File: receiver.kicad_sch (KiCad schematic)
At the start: 146 parts, among them U1 AD8334ACPZ, U4 AD8334ACPZ, U8 TLV9354IDR, U9 TLV9354IDR

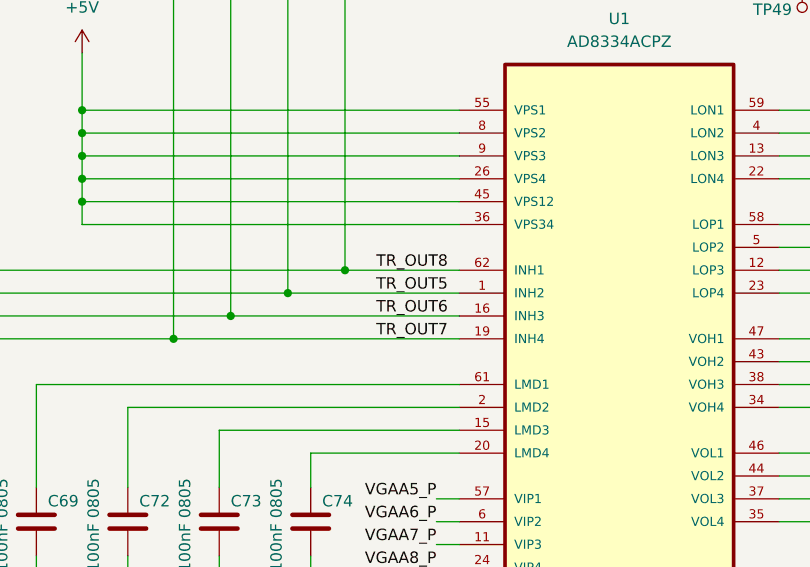
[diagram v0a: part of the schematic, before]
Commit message: 1/4 AFE edits left to go, check if MCU ADC channels could be swapped (use oth ADCs), add voltage monitoring & power planes
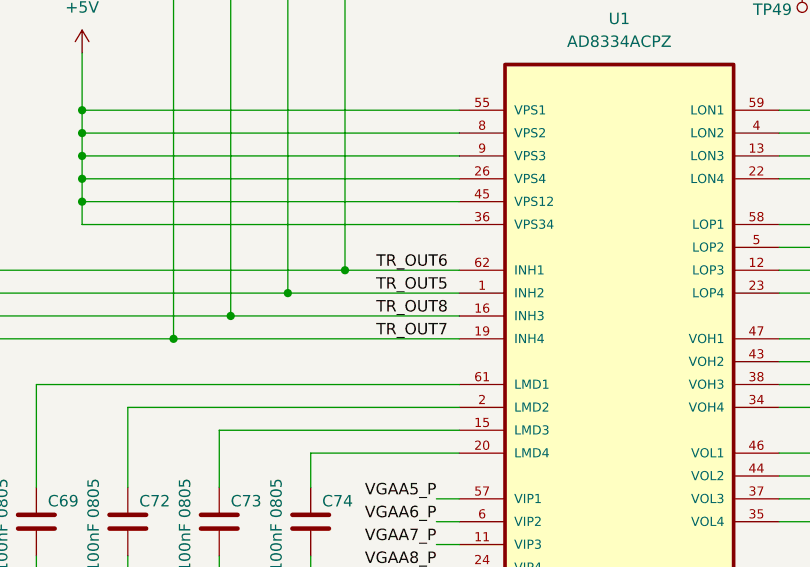
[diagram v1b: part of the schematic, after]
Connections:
- net TR_OUT6: no longer C63.1, R45.1, U1.16 (INH3)
- new net TR_OUT8: C63.1, R45.1, U1.16 (INH3)
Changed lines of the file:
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@@
 	)
 	(label "TR_OUT6"
-		(at 306.07 72.39 180)
+		(at 306.07 67.31 180)
 		(effects
 			(font
@@
 	)
 	(label "TR_OUT8"
-		(at 306.07 67.31 180)
-		(effects
-			(font
+		(at 306.07 72.39 180)
+		(effects
+			(font

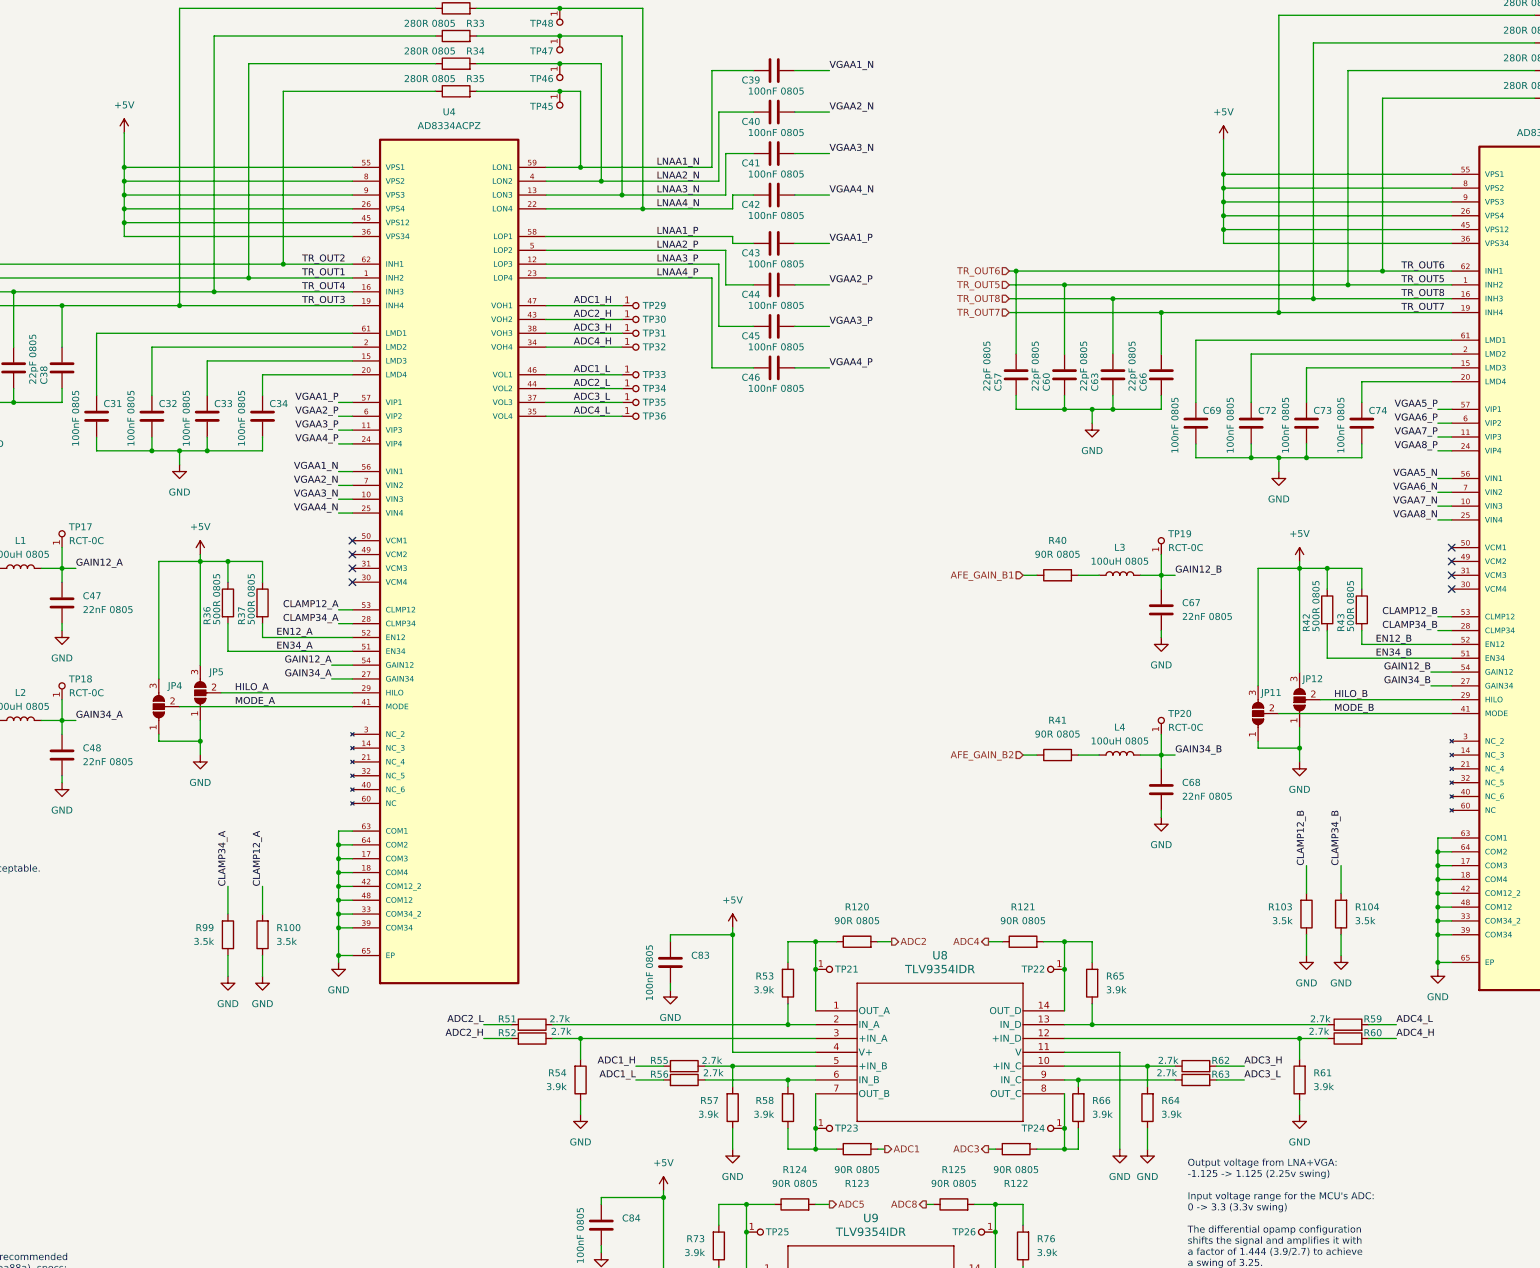
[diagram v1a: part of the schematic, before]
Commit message: 5% left, rearrange ADC channels for right AFE
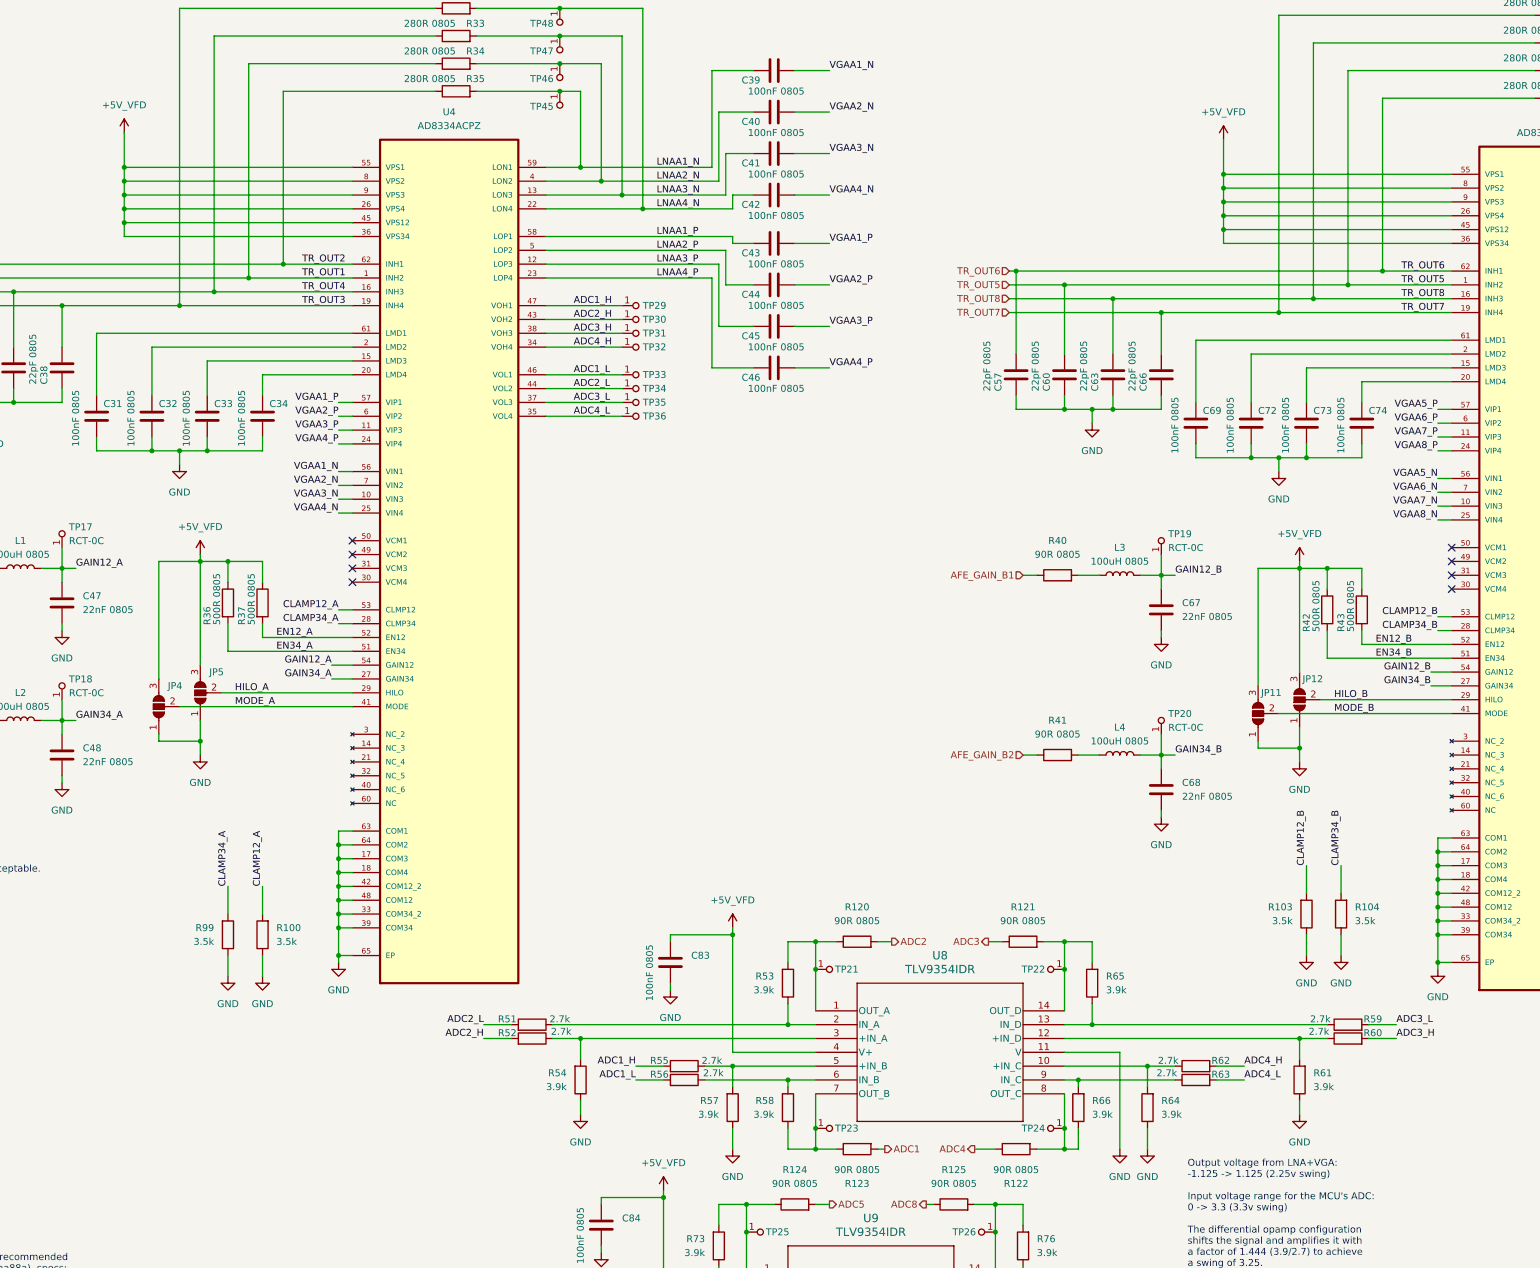
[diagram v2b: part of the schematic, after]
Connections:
- net ADC3: now also R121.1; no longer R122.1
- net ADC3_H: now also R60.2; no longer R62.2
- net ADC3_L: now also R59.2; no longer R63.2
- net ADC4: now also R122.1; no longer R121.1
- net ADC4_H: now also R62.2; no longer R60.2
- net ADC4_L: now also R63.2; no longer R59.2
- net +5V renamed +5V_VFD
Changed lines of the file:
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@@
 	(wire
 		(pts
-			(xy 222.25 228.6) (xy 223.52 228.6)
+			(xy 219.71 228.6) (xy 223.52 228.6)
 		)
 		(stroke
@@
 		)
 	)
+	(label "ADC3_H"
+		(at 297.18 208.28 0)
+		(effects
+			(font
+				(size 1.27 1.27)
+			)
+			(justify left bottom)
+		)
+	)
 	(label "VGAA1_N"
 		(at 102.87 104.14 180)
@@
 		)
 	)
-	(label "ADC3_L"
-		(at 269.24 215.9 0)
-		(effects
-			(font
-				(size 1.27 1.27)
-			)
-			(justify left bottom)
-		)
-	)
 	(label "CLAMP12_A"
 		(at 102.87 129.54 180)
@@
 		)
 	)
-	(label "LNAA3_P"
-		(at 161.29 66.04 0)
+	(label "ADC4_L"
+		(at 269.24 215.9 0)
 		(effects
 			(font
@@
 		)
 	)
-	(label "ADC7_L"
-		(at 256.54 264.16 0)
+	(label "LNAA3_P"
+		(at 161.29 66.04 0)
 		(effects
 			(font
@@
 	)
 	(label "ADC7_L"
-		(at 347.98 92.71 0)
+		(at 256.54 264.16 0)
 		(effects
 			(font
@@
 		)
 	)
-	(label "ADC3_H"
-		(at 269.24 213.36 0)
+	(label "ADC7_L"
+		(at 347.98 92.71 0)
 		(effects
 			(font
@@
 		)
 	)
-	(label "ADC4_L"
-		(at 297.18 205.74 0)
-		(effects
-			(font
-				(size 1.27 1.27)
-			)
-			(justify left bottom)
-		)
-	)
 	(label "GAIN12_B"
 		(at 303.53 140.97 180)
@@
 		)
 	)
+	(label "ADC4_H"
+		(at 269.24 213.36 0)
+		(effects
+			(font
+				(size 1.27 1.27)
+			)
+			(justify left bottom)
+		)
+	)
 	(label "CLAMP34_A"
 		(at 102.87 132.08 180)
@@
 		)
 	)
-	(label "ADC4_H"
-		(at 297.18 208.28 0)
-		(effects
-			(font
-				(size 1.27 1.27)
-			)
-			(justify left bottom)
-		)
-	)
 	(label "ADC3_H"
 		(at 146.05 78.74 0)
@@
 		)
 	)
+	(label "ADC3_L"
+		(at 297.18 205.74 0)
+		(effects
+			(font
+				(size 1.27 1.27)
+			)
+			(justify left bottom)
+		)
+	)
 	(label "ADC5_L"
 		(at 116.84 254 180)
@@
 	(hierarchical_label "ADC3"
 		(shape output)
-		(at 222.25 228.6 180)
+		(at 222.25 190.5 180)
 		(effects
 			(font
@@
 	(hierarchical_label "ADC4"
 		(shape output)
-		(at 222.25 190.5 180)
+		(at 219.71 228.6 180)
 		(effects
 			(font
@@
 			)
 		)
-		(property "Value" "+5V"
+		(property "Value" "+5V_VFD"
 			(at 279.4 115.57 0)
 			(effects
@@
 			)
 		)
-		(property "Value" "+5V"
+		(property "Value" "+5V_VFD"
 			(at 77.47 114.3 0)
 			(effects
@@
 			)
 		)
-		(property "Value" "+5V"
+		(property "Value" "+5V_VFD"
 			(at 162.56 231.14 0)
 			(effects
@@
 			)
 		)
-		(property "Value" "+5V"
+		(property "Value" "+5V_VFD"
 			(at 175.26 182.88 0)
 			(effects
@@
 			)
 		)
-		(property "Value" "+5V"
+		(property "Value" "+5V_VFD"
 			(at 63.5 36.83 0)
 			(effects
@@
 			)
 		)
-		(property "Value" "+5V"
+		(property "Value" "+5V_VFD"
 			(at 265.43 38.1 0)
 			(effects

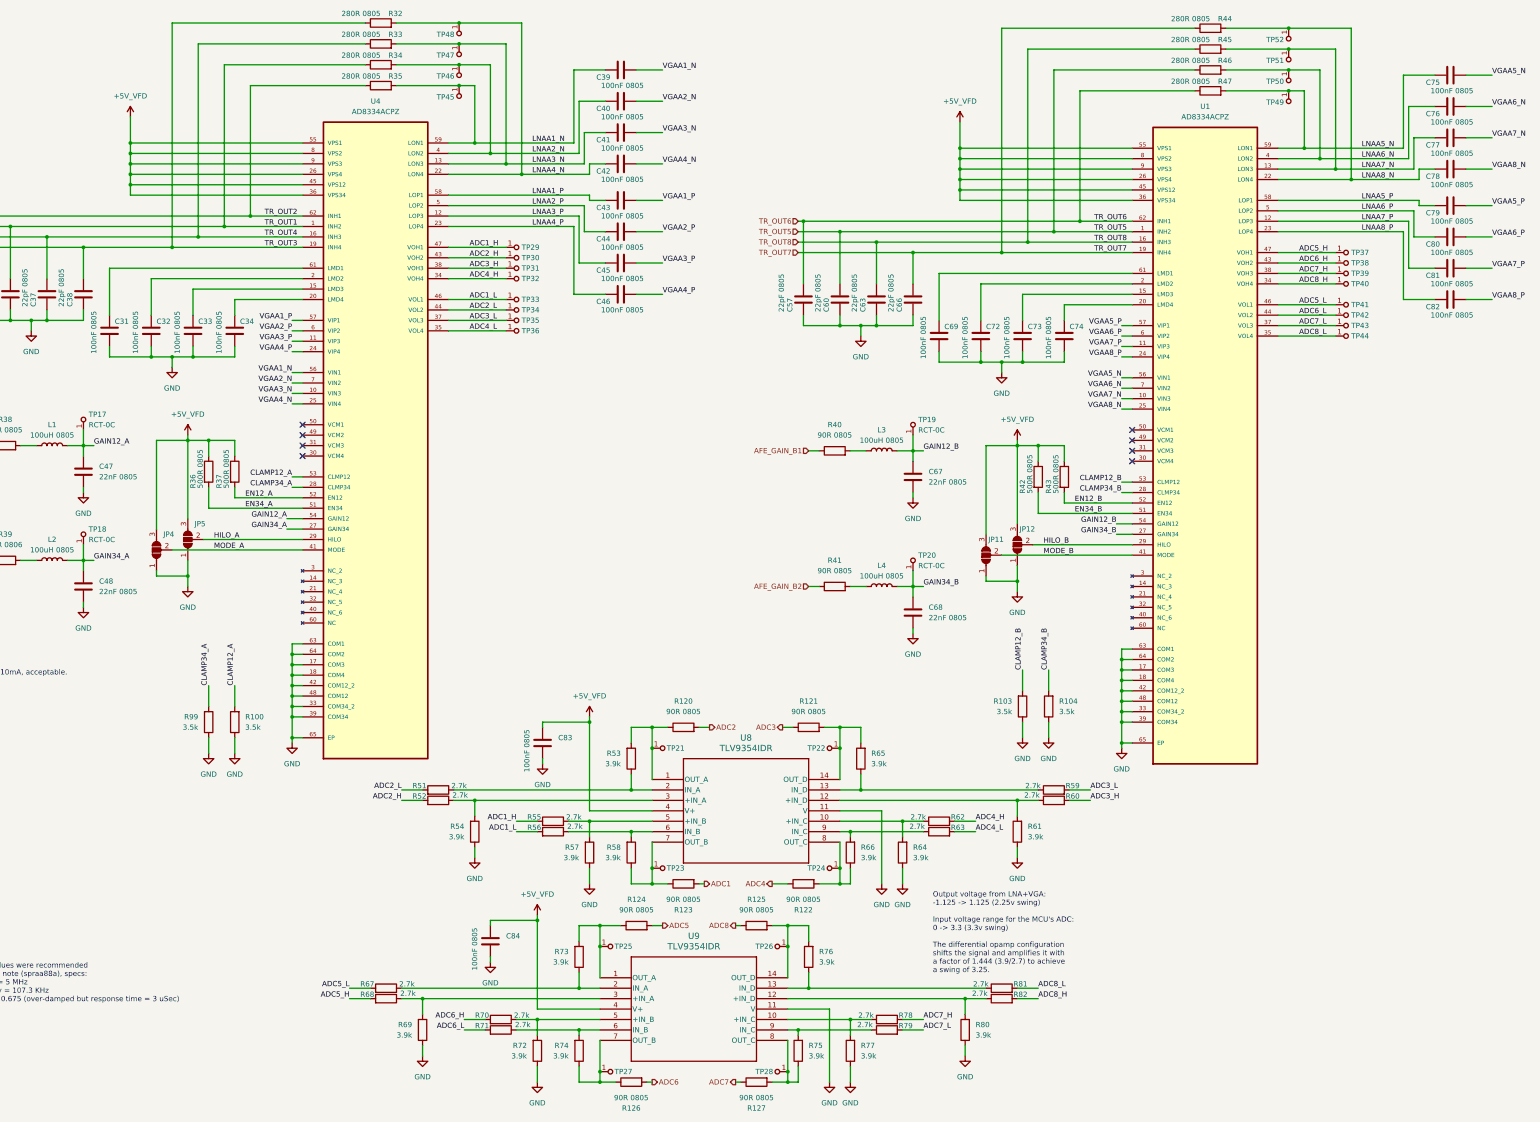
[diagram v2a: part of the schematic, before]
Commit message: added test points & fuse
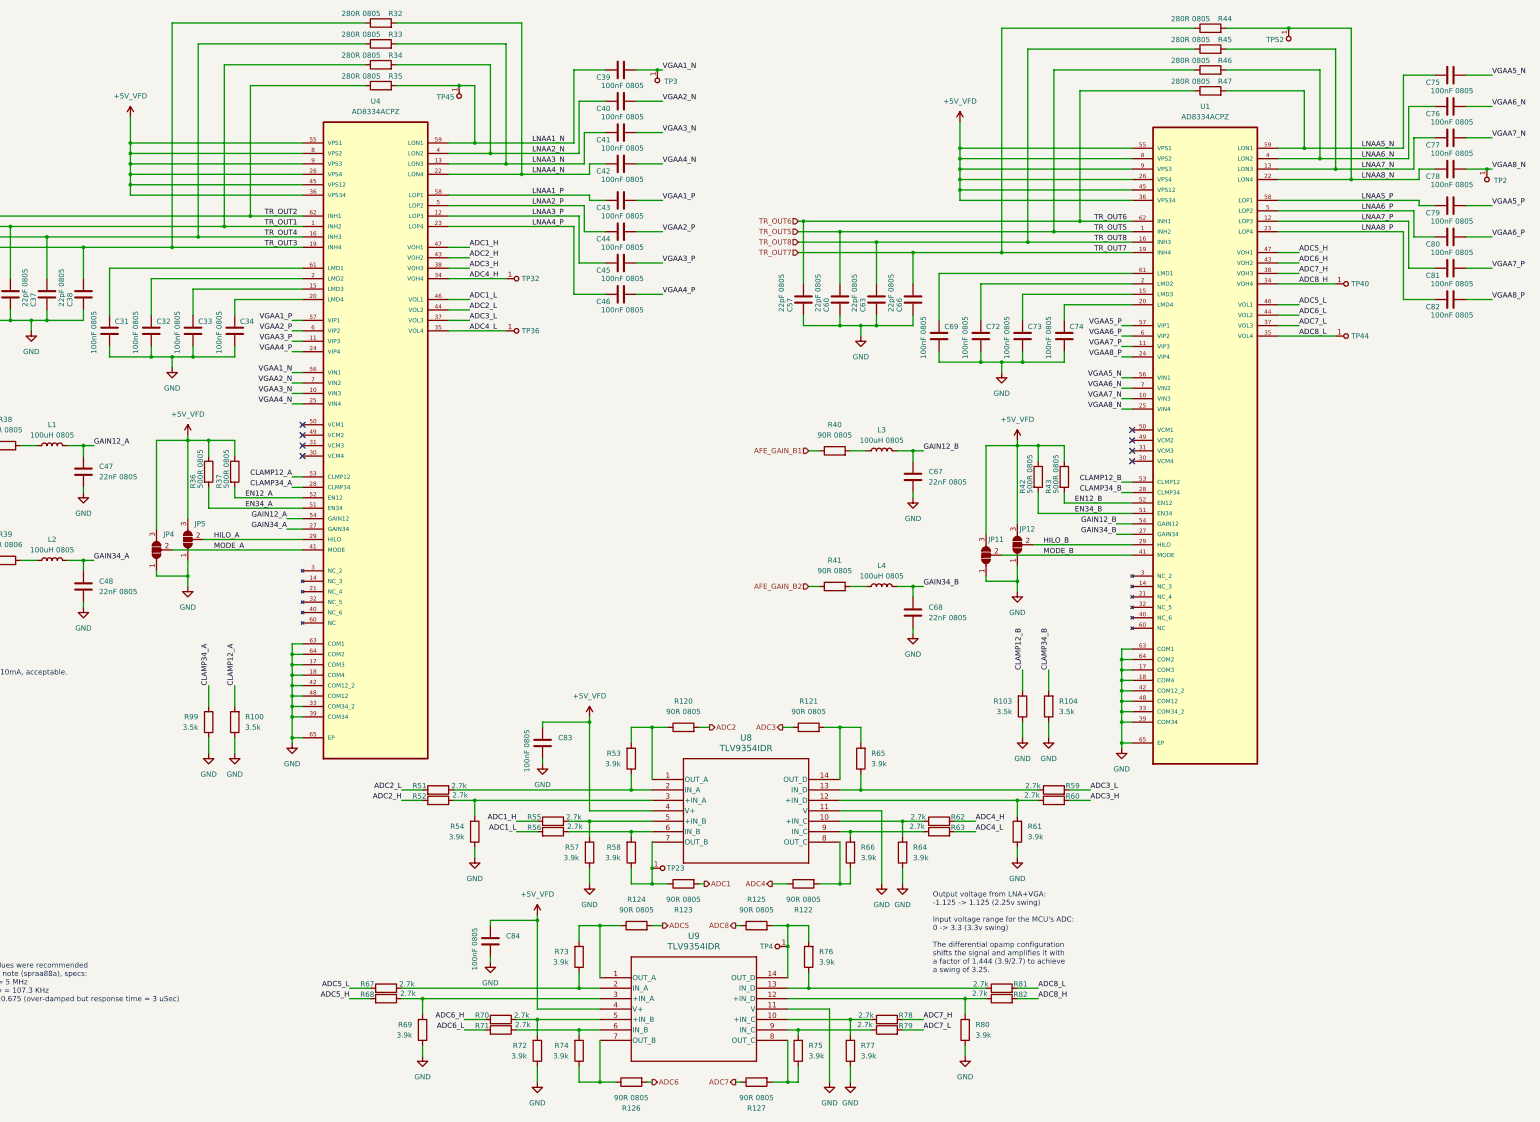
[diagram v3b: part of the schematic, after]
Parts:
- removed TP17, TP18, TP19, TP20, TP21, TP22, TP24, TP25, TP26, TP27, TP28, TP29, TP30, TP31, TP33, TP34, TP35, TP37, TP38, TP39, TP41, TP42, TP43, TP46, TP47, TP48, TP49, TP50, TP51: RCT-0C, digikey-footprints:PROBE_PAD_0805, symbol dk_Test-Points:RCT-0C
- added TP2, TP3, TP4: RCT-0C, digikey-footprints:PROBE_PAD_0805, symbol dk_Test-Points:RCT-0C
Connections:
- net VGAA1_N: now also TP3.1
- net VGAA8_N: now also TP2.1
- net at R125.2, R76.2, U9.14 (OUT_D): now also TP4.1
